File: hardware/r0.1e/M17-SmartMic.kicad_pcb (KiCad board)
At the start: 4 copper layers, 84.9 x 89.9 mm, 178 parts, among them IC1 LM4861M, J1 Kenwood-2.5, J10 UART, J11 Radio_Opt, J12 Speaker, J2 USB_C, J3 OLED, J4 CAT_TX, J5 Kenwood-3.5, J6 CAT_TX, J7 Radio, J8 +12V, J9 STLink, Q1 IRLML2060, Q2 BSS138, Q3 BSS138, SW1 Button Up, SW2 Button Down, SW3 Reset, SW4 Button Escape, SW5 Button Left, SW6 Button Enter, SW7 Button Right, U1 MAX9814, U10 STM32F405RGTx, U11 TPS73233, U2 TP6841S6, U3 USBLC6-2, U6 MCP6002, U7 MCP6002, X1 12 MHz TCXO, Y1 8 MHz

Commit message: WIP r0.1e power switch
👀
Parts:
- removed RV1: 50k, M17-SmartMic:PTR901
- added RV4: 10k, Potentiometer_THT:Potentiometer_Alps_RK097_Single_Horizontal, F.Cu at (85.6, 118.9)
- moved J10 37.7 mm to (71.9, 70.9)
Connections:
- FB2 pad 2: Net-(FB2-Pad2) -> unconnected-(FB2-Pad2)
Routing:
- net Net-(FB2-Pad2): track 129.1 -> 0.00 mm, vias 1 -> 0
- net VIN: track 176.4 -> 52.2 mm
- net USART1_RX: track 16.4 -> 29.7 mm
- net USART1_TX: track 20.7 -> 28.9 mm
- net +5V: track 198.1 -> 202.3 mm
- net unconnected-(FB2-Pad2): track 0.00 -> 1.17 mm, vias 0 -> 1
- net +12V: track 131.3 -> 130.3 mm
- net GND: vias 61 -> 63
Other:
- board text added: "DB9MAT, SP5WWP"
- board text added: "Revision 0.1e 04.2023"
- board text removed: "Revision 0.1e 04.2023 DB9MAT, SP5WWP"

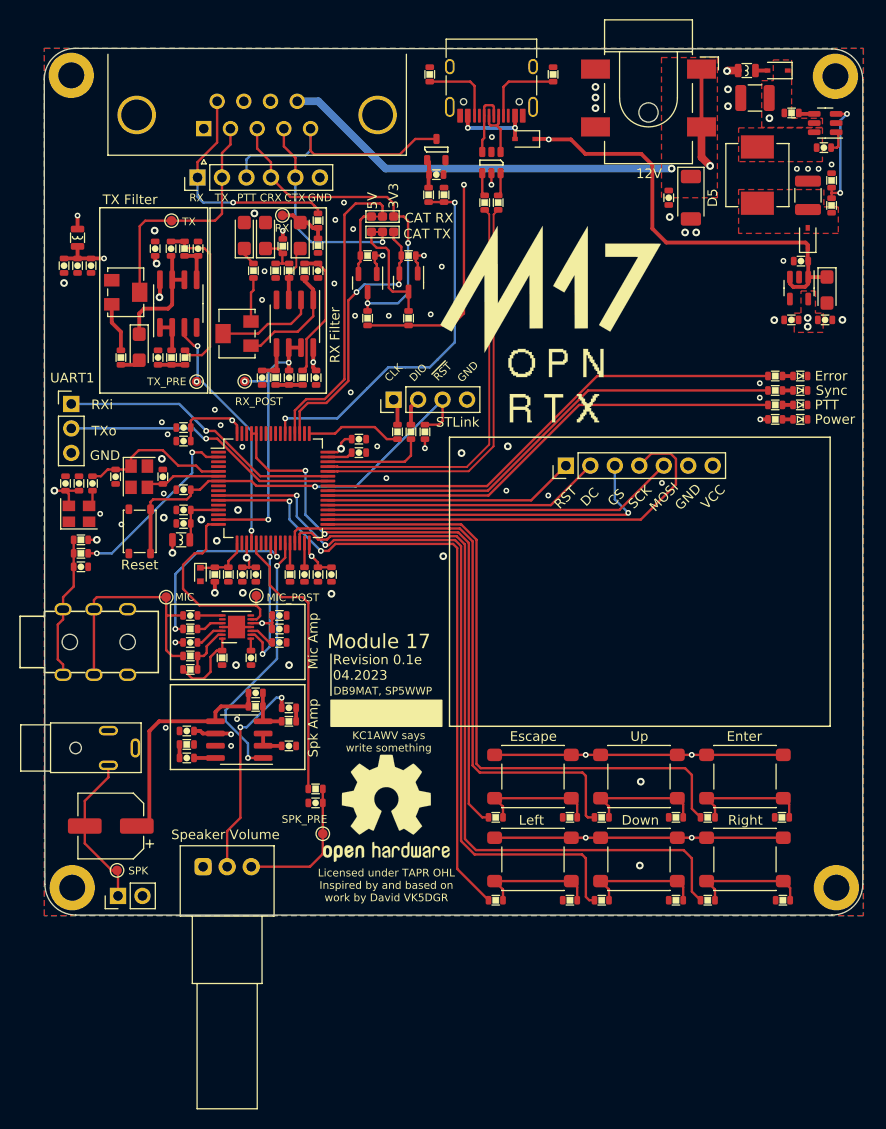
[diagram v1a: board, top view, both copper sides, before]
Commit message: Updates to the latching power switch
WIP r0.1e, schematics can be considered final
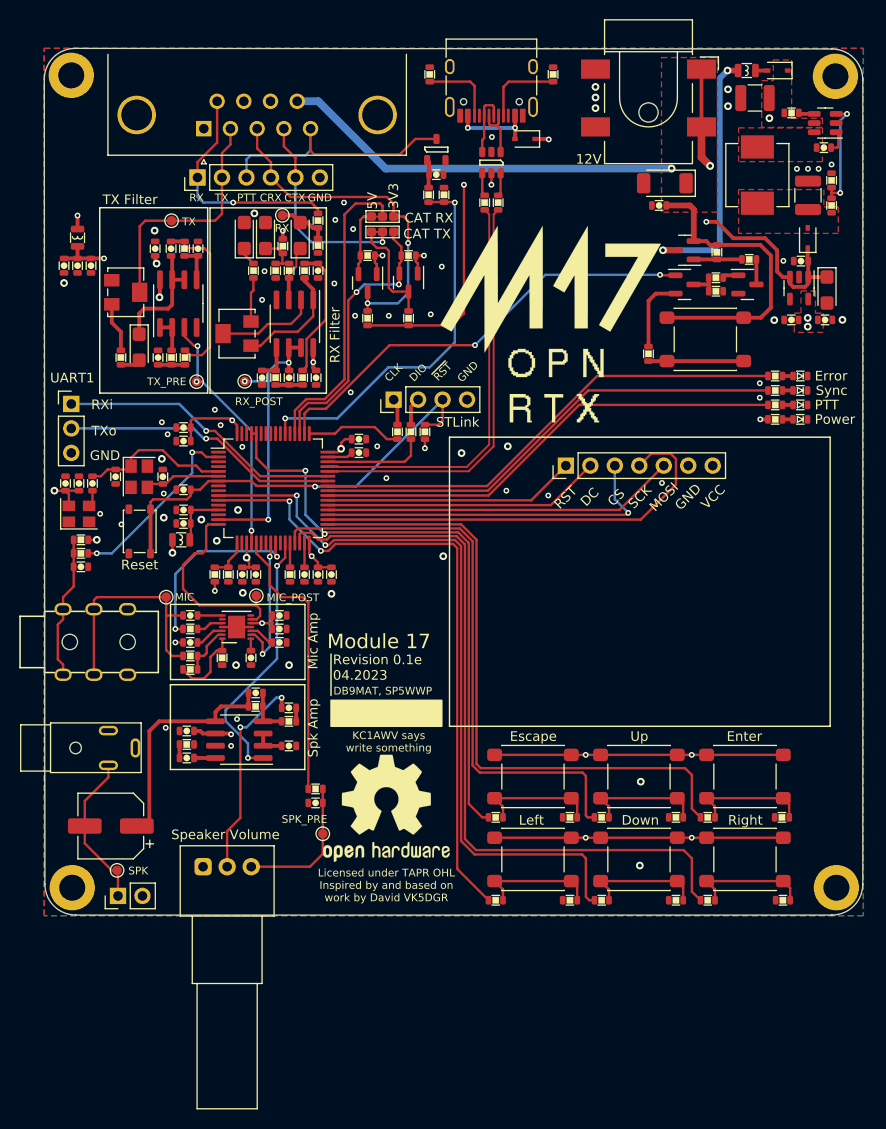
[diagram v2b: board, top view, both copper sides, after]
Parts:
- removed D10: 3v3, Diode_SMD:D_SOD-523
- added D7: BAT54C, Package_TO_SOT_SMD:SOT-23, F.Cu at (135.5, 58.5)
- added Q4: IRLML2244, Package_TO_SOT_SMD:SOT-23, F.Cu at (135.6, 55.0)
- added Q5: MMBT3904, Package_TO_SOT_SMD:SOT-23, F.Cu at (142.1, 58.5)
- added R63: 100k, pkl_dipol:R_0603, F.Cu at (131.8, 65.7)
- added R64: 10k, pkl_dipol:R_0603, F.Cu at (138.8, 57.8)
- added R65: 100k, pkl_dipol:R_0603, F.Cu at (138.8, 59.2)
- added R66: 22k, pkl_dipol:R_0603, F.Cu at (138.9, 55.1)
- added R67: 22k, pkl_dipol:R_0603, F.Cu at (142.2, 55.9)
- added SW8: Button Power, pkl_buttons_switches:SW_SPST_PTS645, F.Cu at (137.7, 64.2)
- moved D5 3.09 mm to (133.5, 48.0), turned to 180 degrees
- moved C61 1.28 mm to (132.9, 50.3), turned to 0 degrees
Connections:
- FB2 pad 2: unconnected-(FB2-Pad2) -> Net-(Q4-D)
- R53 pad 1: +12V -> VDD
- U10 pad 26: FLASH_CS -> unconnected-(U10-PB0-Pad26)
- U10 pad 3: Net-(U10-PC14) -> unconnected-(U10-PC14-Pad3)
- U10 pad 4: Net-(U10-PC15) -> unconnected-(U10-PC15-Pad4)
- U10 pad 50: unconnected-(U10-PA15-Pad50) -> GPIO_POWER
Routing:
- net +12V: track 130.3 -> 0.00 mm, vias 2 -> 1
- net GPIO_POWER: track 0.00 -> 46.6 mm, vias 0 -> 2
- net VIN: track 52.2 -> 83.7 mm
- net Net-(Q4-D): track 0.00 -> 26.9 mm, vias 0 -> 2
- net Net-(R63-Pad1): track 0.00 -> 9.88 mm
- net Net-(D7-Pad2): track 0.00 -> 7.86 mm
- net Net-(Q4-G): track 0.00 -> 5.00 mm
- net +5V: track 202.3 -> 197.6 mm, vias 5 -> 6
- net Net-(D7-Pad3): track 0.00 -> 2.98 mm
- net Net-(Q5-C): track 0.00 -> 2.60 mm
- net Net-(Q5-B): track 0.00 -> 1.68 mm
- net Net-(U10-PA3): track 5.82 -> 4.37 mm
- net unconnected-(FB2-Pad2): track 1.17 -> 0.00 mm, vias 1 -> 0
- net VDD: track 98.2 -> 99.1 mm, vias 19 -> 20
- net GND: vias 63 -> 60

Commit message: Gold Master r0.1e
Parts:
- removed D6: BAT60A, Diode_SMD:D_SOD-323
- removed R62: 1k, pkl_dipol:R_0603
- R42: value 10k -> 2k2
- R53: value 39k -> 2k7
- moved C57 11.6 mm to (78.4, 53.4), turned to 90 degrees
- moved RV3 1.35 mm to (77.5, 60.7)
- moved FB2 1.10 mm to (143.1, 36.3)
- turned R65 to 180 degrees
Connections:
- C57 pad 2: Net-(C57-Pad2) -> RADIO_TX
- FB2 pad 1: Net-(D6-A) -> +12V
- R65 pad 1: Net-(D7-Pad3) -> Net-(Q5-B)
- RV3 pad 2: RADIO_TX -> Net-(U6A-+)
- RV3 pad 3: Net-(R62-Pad2) -> BASEBAND_TX
- U6 pad 3: BASEBAND_TX -> Net-(U6A-+)
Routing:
- net OLED_SPI_SCK: track 44.8 -> 34.9 mm, vias 0 -> 1
- net BASEBAND_TX: track 25.9 -> 34.1 mm, vias 3 -> 2
- net Net-(U6A-+): track 0.00 -> 6.66 mm
- net RADIO_TX: track 25.1 -> 18.5 mm
- net Net-(R62-Pad2): track 5.17 -> 0.00 mm
- net VIN: track 83.7 -> 79.3 mm, vias 2 -> 1
- net Net-(U6B--): track 12.3 -> 8.30 mm
- net OLED_CS: track 36.7 -> 32.8 mm
- net OLED_SPI_MOSI: track 36.8 -> 40.6 mm, vias 0 -> 1
- net USB_DN: track 43.0 -> 40.0 mm
- net USB_DP: track 42.3 -> 39.3 mm
- net Net-(C57-Pad2): track 2.10 -> 0.00 mm
- net BTN_UP: track 60.9 -> 59.0 mm, vias 0 -> 2
- net BTN_ENT: track 66.9 -> 65.1 mm, vias 0 -> 2
- net ~{BOOT0}: track 61.3 -> 59.6 mm
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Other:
- board text added: "Revision 0.1e 05.2023"
- board text removed: "Revision 0.1e 04.2023"

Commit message: r0.1e PCBA files
specifically for JLCPCB
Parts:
- R24, R25, R26, R27: value 680R -> 680
- R56: value 24k -> 8k2
- R57: value 126k -> 43k
- U11: value TPS73233 -> TPS7A2033
